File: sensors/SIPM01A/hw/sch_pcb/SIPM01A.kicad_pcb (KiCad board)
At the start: 2 copper layers, 60.5 x 40.1 mm, 33 parts, among them J1 HEADER_2x04_PARALLEL, M1 HOLE, M2 HOLE, M3 HOLE, M4 HOLE, U1 ARRAYC-60035-4P-BGA

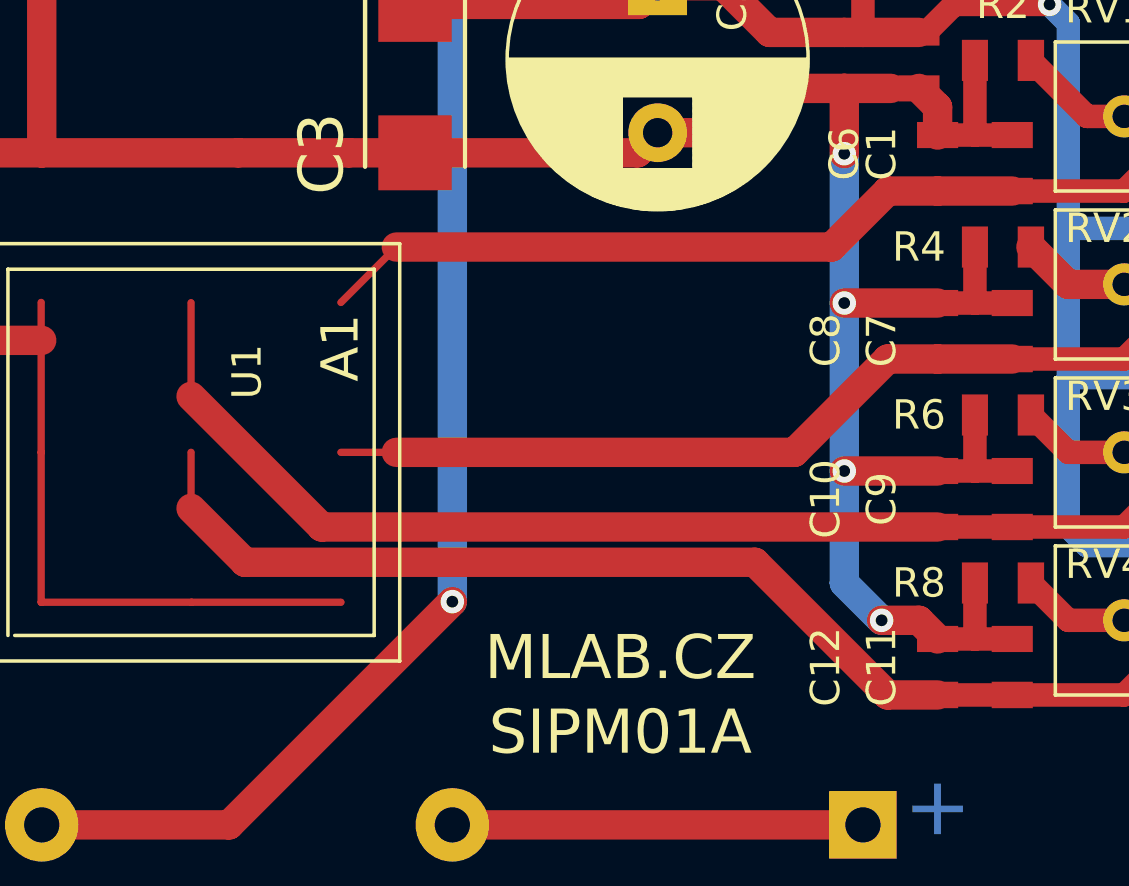
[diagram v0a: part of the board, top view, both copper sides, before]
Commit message: Přidání plošek pro odpojení napájení
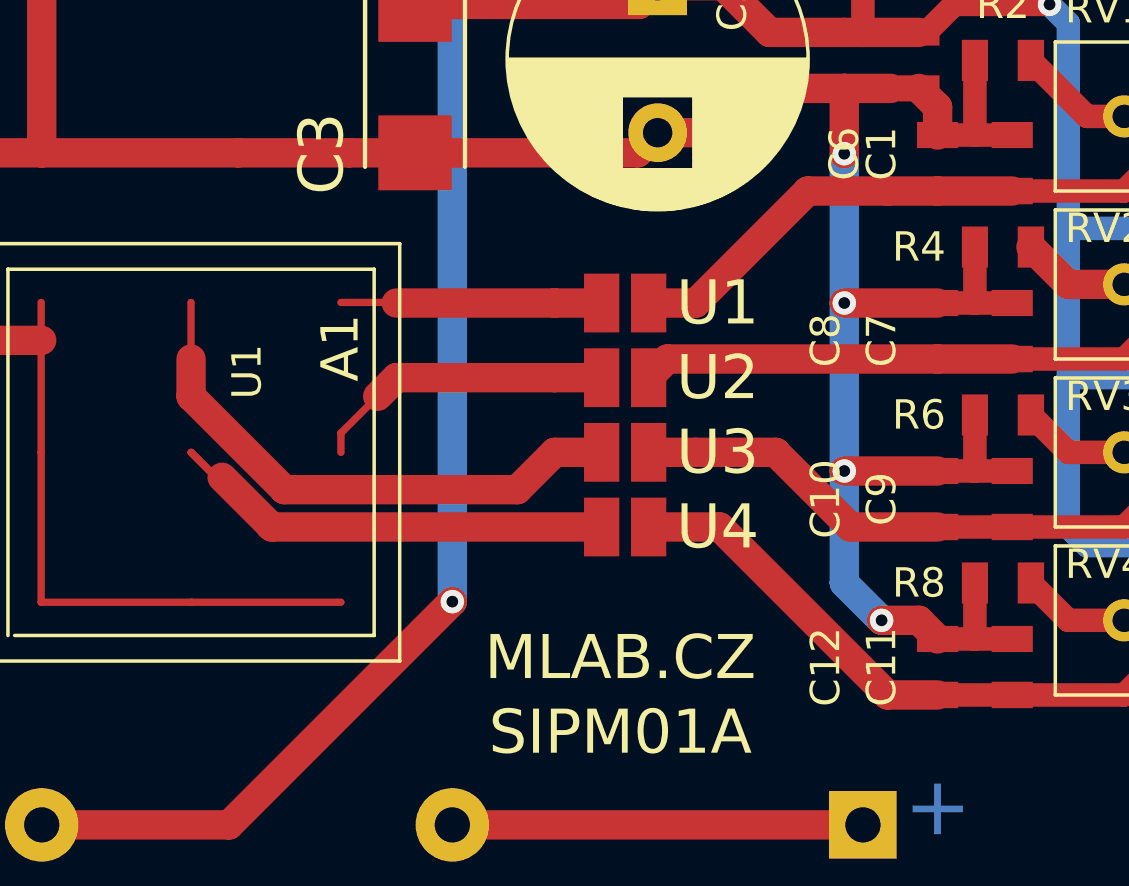
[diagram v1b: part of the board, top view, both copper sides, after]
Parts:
- added J2: JUMP2_2x1, Mlab_Pin_Headers:Zkrat, F.Cu at (34.9, -22.2)
- added J3: JUMP2_2x1, Mlab_Pin_Headers:Zkrat, F.Cu at (34.9, -19.7)
- added J4: JUMP2_2x1, Mlab_Pin_Headers:Zkrat, F.Cu at (34.9, -17.1)
- added J5: JUMP2_2x1, Mlab_Pin_Headers:Zkrat, F.Cu at (34.9, -14.6)
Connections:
- U1 pad A1: /U1 -> Net-(J2-Pad1)
- U1 pad A2: /U2 -> Net-(J3-Pad1)
- U1 pad B1: /U3 -> Net-(J4-Pad1)
- U1 pad B2: /U4 -> Net-(J5-Pad1)
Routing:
- net Net-(J5-Pad1): track 0.00 -> 30.0 mm
- net /U3: track 40.4 -> 20.8 mm
- net Net-(J4-Pad1): track 0.00 -> 19.0 mm
- net /U4: track 39.9 -> 22.1 mm
- net /U2: track 31.6 -> 20.0 mm
- net /U1: track 31.8 -> 21.4 mm
- net Net-(J3-Pad1): track 0.00 -> 10.3 mm
- net Net-(J2-Pad1): track 0.00 -> 8.88 mm
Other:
- board text added: "U1"
- board text added: "U2"
- board text added: "U3"
- board text added: "U4"
